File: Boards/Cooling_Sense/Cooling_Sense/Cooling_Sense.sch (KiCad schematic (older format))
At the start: 29 parts, among them J1 CONN_02X03, U1 MCP2561-E_SN, U101 TPS560430YF, U2 ATMEGA16M1, Y1 Crystal_SMD

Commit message: started layout
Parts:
- added D1, D2, D3, D4, D5, D6: LED_0805, footprints:LED_0805_OEM, symbol formula:LED_0805
- added J2: MM_F_RA_20, footprints:micromatch_female_ra_20, symbol formula:MM_F_RA_20
- added Q1: SSM3K333R, footprints:SOT-23F, symbol formula:SSM3K333R
- added R4, R5, R6, R7, R8, R9: R_200, footprints:R_0805_OEM, symbol formula:R_200
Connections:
- net 12V: now also J2.2
- net CAN_HI: now also J2.3
- net CAN_LO: now also J2.4
- net GND: now also D1.1 (K), D2.1 (K), D3.1 (K), D4.1 (K), D5.1 (K), D6.1 (K), J2.1, Q1.2 (S)
- net TEMP_STATUS: now reaches U2.13 ((PCINT21/ADC2/ACMP2)PD5)
- net TEMP_STATUS: now also R5.1
- net PRESSURE_STATUS: now reaches U2.14 ((PCINT22/ADC3/INT0/ACMPN2)PD6)
- net PRESSURE_STATUS: now also R6.1
- net RADIATOR_TEMP_SENSE: now reaches U2.16 ((PCINT2/ADC5/INT1/ACMPN0)PB2)
- net RADIATOR_TEMP_SENSE: now also J2.5
- net CONTROLLER_PRESSURE_SENSE: now reaches U2.17 ((PCINT12/ADC8/ACMPN3/AMP1-)PC4)
- net CONTROLLER_PRESSURE_SENSE: now also J2.9
- net PUMP_CONTROL: now reaches U2.18 ((PCINT13/ADC9/ACMP3/AMP1+)PC5)
- net PUMP_CONTROL: now also Q1.1 (G)
- net COOLING_ACTIVE: now reaches U2.22 ((PCINT14/ADC10/ACMP1)PC6)
- net COOLING_ACTIVE: now also R4.1
- net LED_3: now reaches U2.23 ((PCINT3/AMP0-)PB3)
- net LED_3: now also R9.1
- net MOTOR_TEMP_SENSE: now reaches U2.26 ((PCINT5/ADC6/INT2/ACMPN1/AMP2-)PB5)
- net MOTOR_TEMP_SENSE: now also J2.6
- net CONTROLLER_TEMP_SENSE: now reaches U2.27 ((PCINT6/ADC7/PSCOUT1B)PB6)
- net CONTROLLER_TEMP_SENSE: now also J2.7
- net PUMP_PRESSURE_SENSE: now reaches U2.28 ((PCINT7/ADC4/SCK/PSCOUT0B)PB7)
- net PUMP_PRESSURE_SENSE: now also J2.8
- net LED_1: now reaches U2.8 ((PCINT0/MISO/PSCOUT2A)PB0)
- net LED_1: now also R7.1
- net LED_2: now reaches U2.9 ((PCINT1/MOSI/PSCOUT2B)PB1)
- net LED_2: now also R8.1
- new net: D1.2 (A), R4.2
- new net: D2.2 (A), R5.2
- new net: D3.2 (A), R6.2
- new net: D4.2 (A), R7.2
- new net: D5.2 (A), R8.2
- new net: D6.2 (A), R9.2
- new net PUMP_RELAY: J2.10, Q1.3 (D)
- no-connect marks 2 -> 19
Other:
- note added: "INPUT PINS\n"
- note added: "PROGRAMMING LEDS\n"
- note added: "PUMP CONTROL"
- note added: "SYSTEM STATUS LEDS\n"
- moved on the sheet: C3, R3

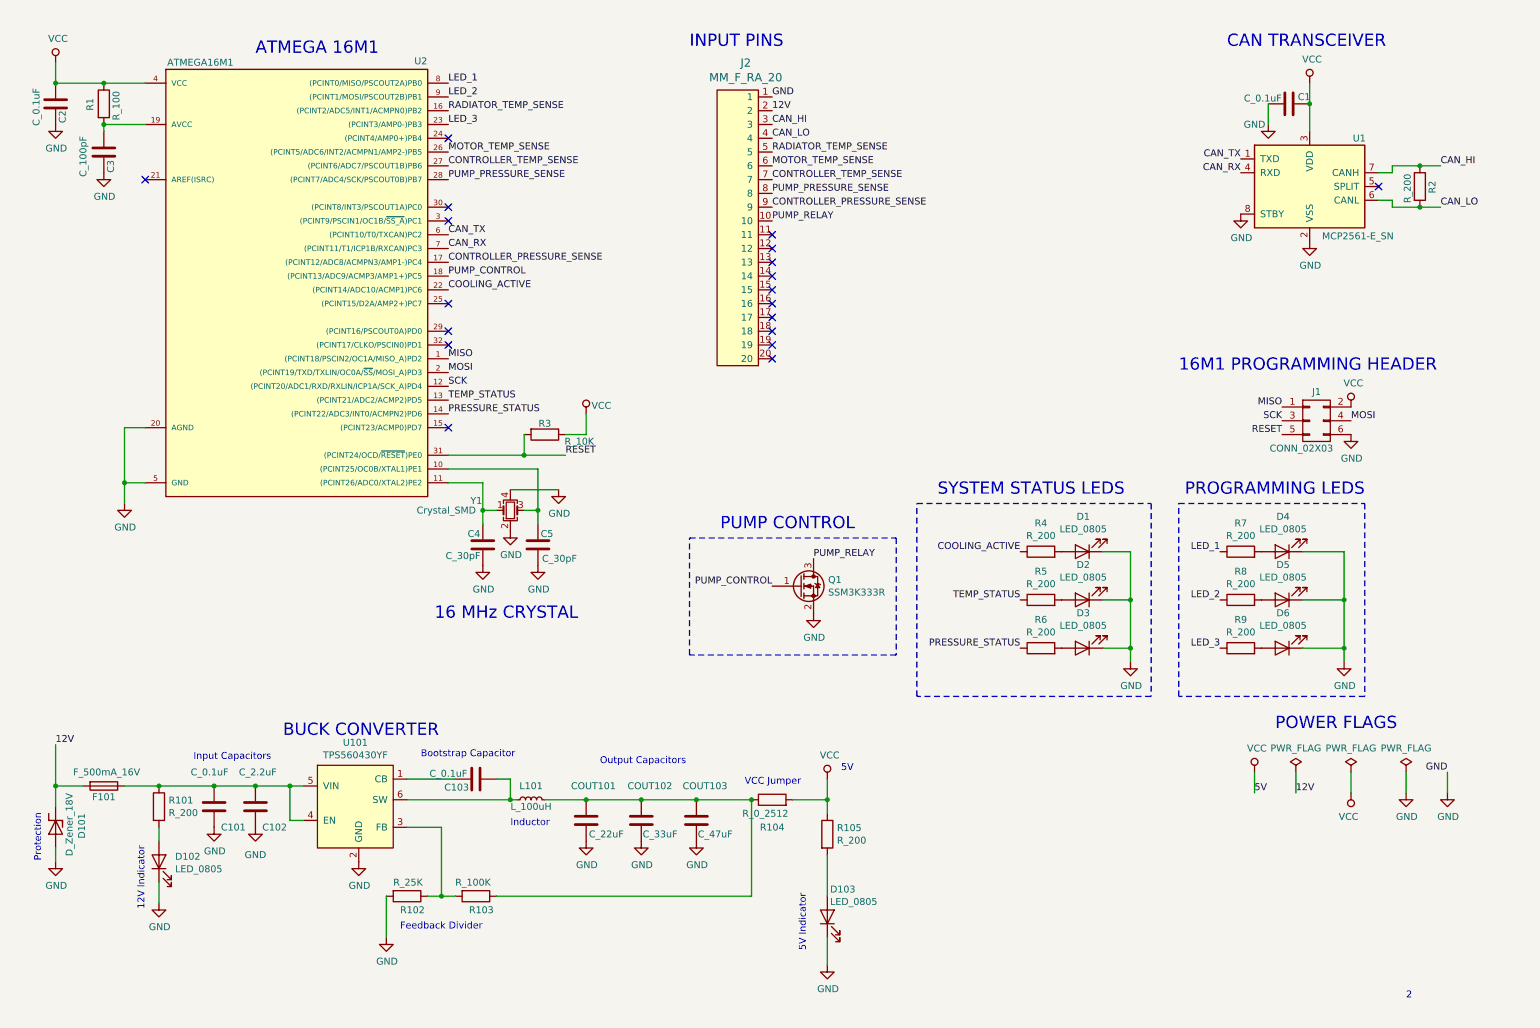
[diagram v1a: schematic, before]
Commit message: began adding sensor check logic circuits, added details (pull down resistors, new wires)
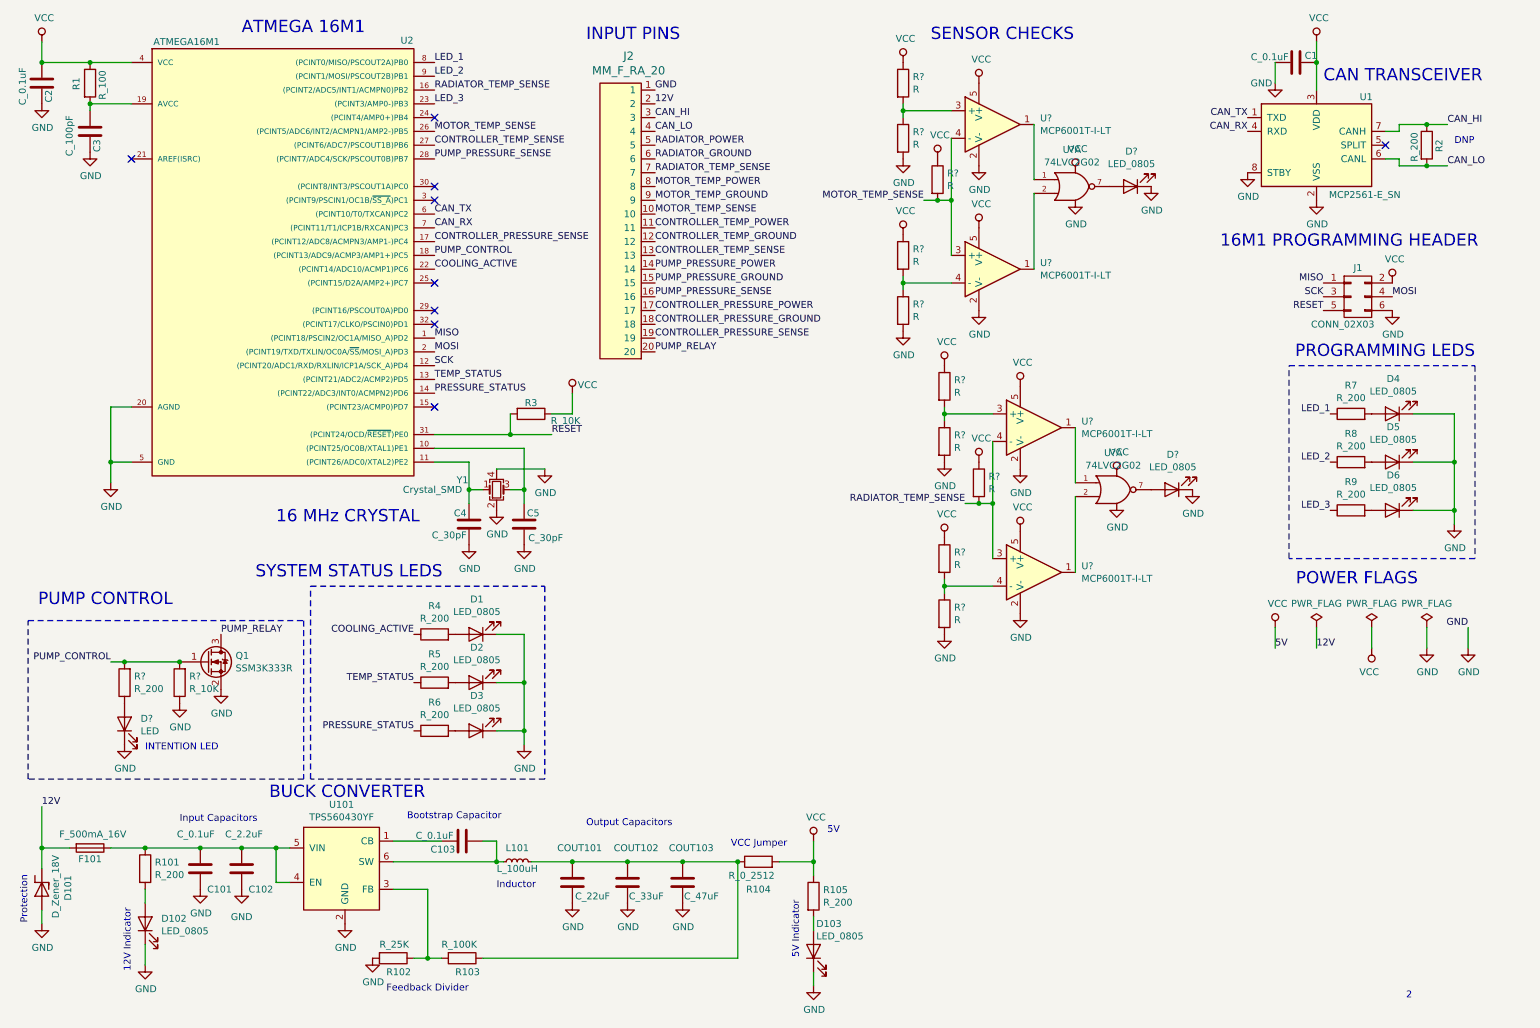
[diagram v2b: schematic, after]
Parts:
- added D?: LED, symbol Device:LED
- added D? (x2): LED_0805, footprints:LED_0805_OEM, symbol formula:LED_0805
- added R?: R_10K, footprints:R_0805_OEM, symbol formula:R_10K
- added R?: R_200, footprints:R_0805_OEM, symbol formula:R_200
- added R? (x10): R, symbol Device:R
- added U? (x4): MCP6001T-I-LT, Package_TO_SOT_SMD:SOT-353_SC-70-5, symbol formula:MCP6001T-I-LT
- added U? (x2): 74LVC2G02, symbol 74xGxx:74LVC2G02
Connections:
- net CONTROLLER_PRESSURE_SENSE: now also J2.19; no longer J2.9
- net CONTROLLER_TEMP_SENSE: now also J2.13; no longer J2.7
- net GND: now also D?.1 (K), D?.1 (K), D?.1 (K), R?.1, R?.2, R?.2, R?.2, R?.2, U?.2 (V-), U?.2 (V-), U?.2 (V-), U?.2 (V-), U?.4 (GND), U?.4 (GND)
- net MOTOR_TEMP_SENSE: now also J2.10, R?.2, U?.3 (+), U?.4 (-); no longer J2.6
- net PUMP_CONTROL: now also R?.2, R?.2
- net PUMP_PRESSURE_SENSE: now also J2.16; no longer J2.8
- net PUMP_RELAY: now also J2.20; no longer J2.10
- net RADIATOR_TEMP_SENSE: now also J2.7, R?.2, U?.3 (+), U?.4 (-); no longer J2.5
- net VCC: now also R?.1, R?.1, R?.1, R?.1, R?.1, R?.1, U?.5 (V+), U?.5 (V+), U?.5 (V+), U?.5 (V+), U?.8 (VCC), U?.8 (VCC)
- net CONTROLLER_TEMP_POWER: now reaches J2.11
- net CONTROLLER_TEMP_GROUND: now reaches J2.12
- net PUMP_PRESSURE_POWER: now reaches J2.14
- net PUMP_PRESSURE_GROUND: now reaches J2.15
- net CONTROLLER_PRESSURE_POWER: now reaches J2.17
- net CONTROLLER_PRESSURE_GROUND: now reaches J2.18
- new net: D?.2 (A), R?.1
- new net: R?.1, R?.2, U?.3 (+) (x2)
- new net: U?.1, U?.1 (x2)
- new net: R?.1, R?.2, U?.4 (-) (x2)
- new net: U?.1, U?.2 (x2)
- new net: D?.2 (A), U?.7 (x2)
- new net MOTOR_TEMP_GROUND: J2.9
- new net MOTOR_TEMP_POWER: J2.8
- new net RADIATOR_GROUND: J2.6
- new net RADIATOR_POWER: J2.5
- no-connect marks 19 -> 9
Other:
- note added: "DNP"
- note added: "INTENTION LED"
- note added: "SENSOR CHECKS\n"
- moved on the sheet: C1, C101, C102, C103, C2, C3, C4, C5, COUT101, COUT102, COUT103, D1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

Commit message: pushing work from last week and a merge
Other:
- note added: "TO DO:\nCreate a new hierarchical sheet\nMove sensor checks logic circuits to new sheet\nMake sure everything still works"
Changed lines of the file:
@@
 Wire Wire Line
 	6300 7550 6300 7450
+Text Notes 5100 4900 0    50   ~ 0
+TO DO:\nCreate a new hierarchical sheet\nMove sensor checks logic circuits to new sheet\nMake sure everything still works
 $EndSCHEMATC

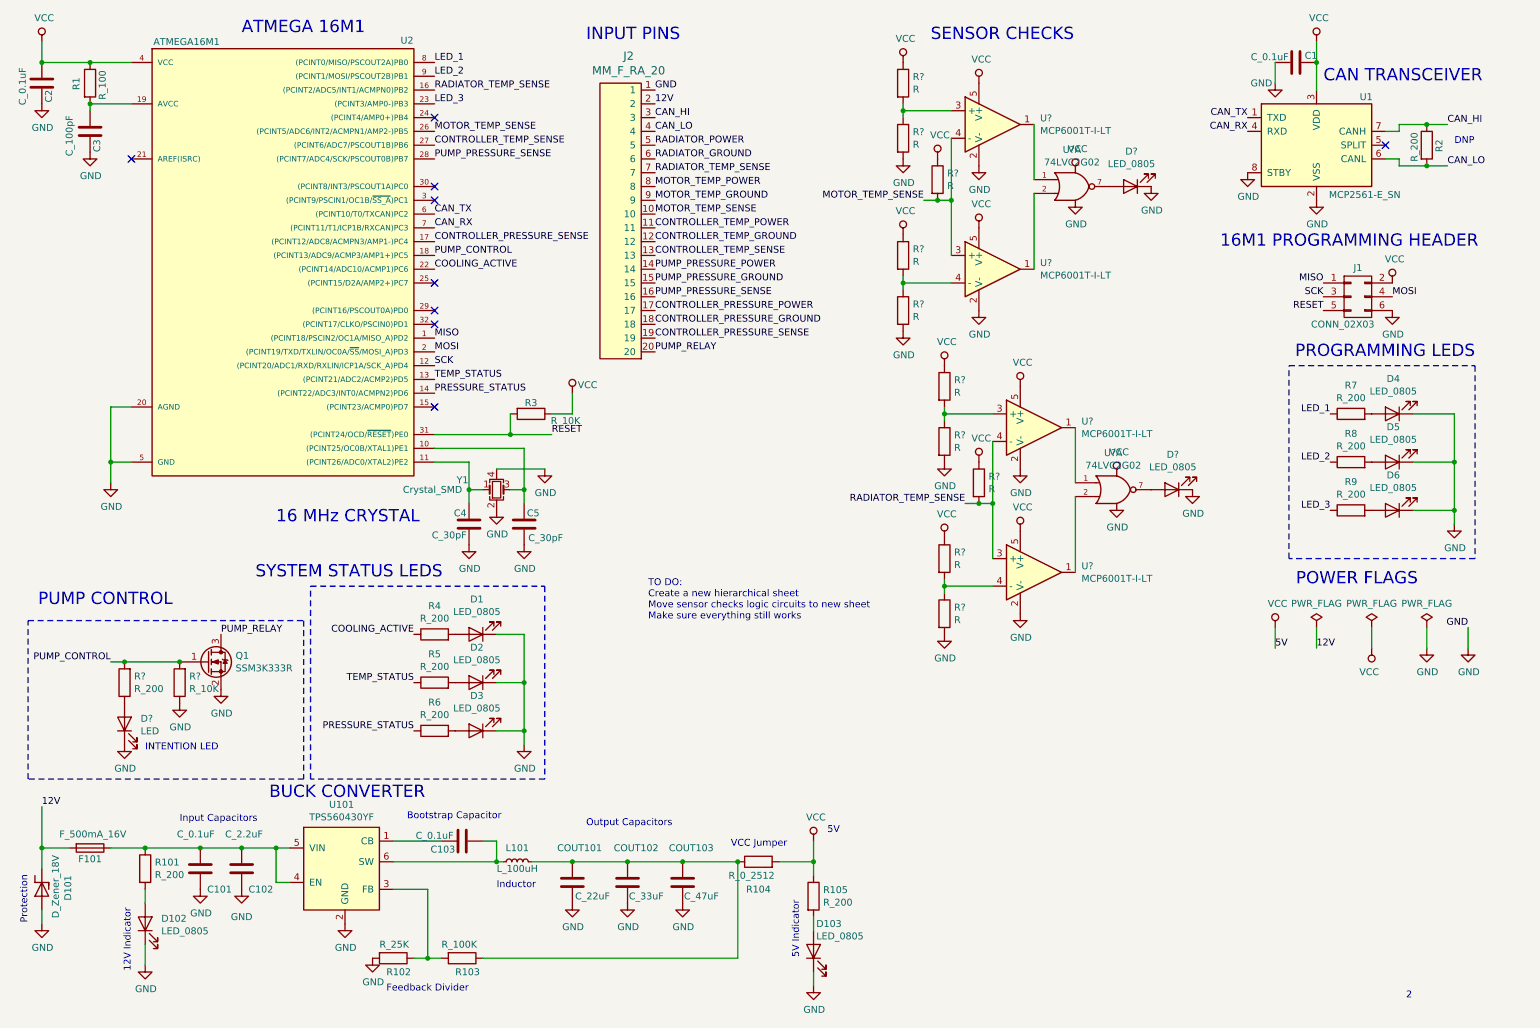
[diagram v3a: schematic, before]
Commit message: Re-added sense check circuits in a new sheet, connected sensor power and ground to power and ground
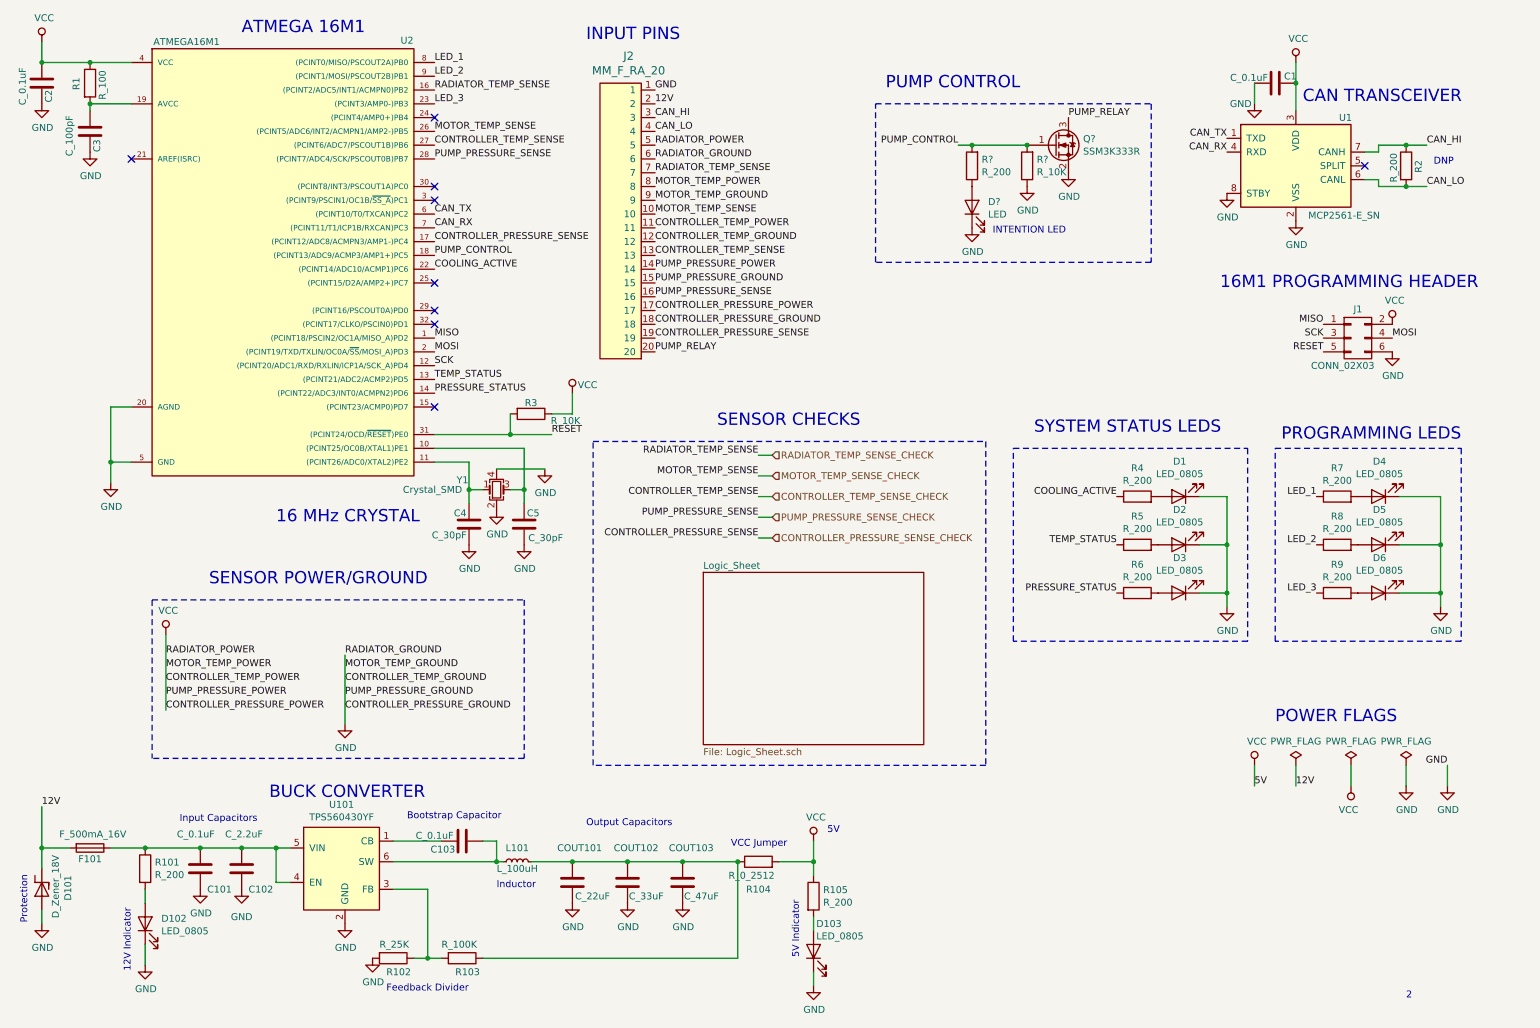
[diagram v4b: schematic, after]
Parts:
- removed D?: LED, symbol Device:LED
- removed D? (x2): LED_0805, footprints:LED_0805_OEM, symbol formula:LED_0805
- removed Q1: SSM3K333R, footprints:SOT-23F, symbol formula:SSM3K333R
- removed R?: R_10K, footprints:R_0805_OEM, symbol formula:R_10K
- removed R?: R_200, footprints:R_0805_OEM, symbol formula:R_200
- removed R? (x10): R, symbol Device:R
- removed U? (x4): MCP6001T-I-LT, Package_TO_SOT_SMD:SOT-353_SC-70-5, symbol formula:MCP6001T-I-LT
- removed U? (x2): 74LVC2G02, symbol 74xGxx:74LVC2G02
- added D?: LED, symbol Device:LED
- added Q?: SSM3K333R, footprints:SOT-23F, symbol formula:SSM3K333R
- added R?: R_10K, footprints:R_0805_OEM, symbol formula:R_10K
- added R?: R_200, footprints:R_0805_OEM, symbol formula:R_200
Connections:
- net CONTROLLER_PRESSURE_GROUND is gone; now on net GND: J2.18
- net CONTROLLER_PRESSURE_POWER is gone; now on net VCC: J2.17
- net CONTROLLER_TEMP_GROUND is gone; now on net GND: J2.12
- net CONTROLLER_TEMP_POWER is gone; now on net VCC: J2.11
- net MOTOR_TEMP_GROUND is gone; now on net GND: J2.9
- net MOTOR_TEMP_POWER is gone; now on net VCC: J2.8
- net PUMP_PRESSURE_GROUND is gone; now on net GND: J2.15
- net PUMP_PRESSURE_POWER is gone; now on net VCC: J2.14
- net RADIATOR_GROUND is gone; now on net GND: J2.6
- net RADIATOR_POWER is gone; now on net VCC: J2.5
- net GND: now also D?.1 (K), Q?.2 (S), R?.1
- net PUMP_CONTROL: now also Q?.1 (G), R?.2, R?.2
- net PUMP_RELAY: now also Q?.3 (D)
- net CONTROLLER_PRESSURE_SENSE renamed CONTROLLER_PRESSURE_SENSE_CHECK
- net CONTROLLER_TEMP_SENSE renamed CONTROLLER_TEMP_SENSE_CHECK
- net MOTOR_TEMP_SENSE renamed MOTOR_TEMP_SENSE_CHECK
- net PUMP_PRESSURE_SENSE renamed PUMP_PRESSURE_SENSE_CHECK
- net RADIATOR_TEMP_SENSE renamed RADIATOR_TEMP_SENSE_CHECK
- new net: D?.2 (A), R?.1
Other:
- note added: "SENSOR POWER/GROUND"
- note removed: "TO DO:\nCreate a new hierarchical sheet\nMove sensor checks logic circuits to new sheet\nMake sure everything still works"
- moved on the sheet: C1, D1, D2, D3, D4, D5, D6, J1, R2, R4, R5, R6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
